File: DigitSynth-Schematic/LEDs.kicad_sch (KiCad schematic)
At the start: 0 parts

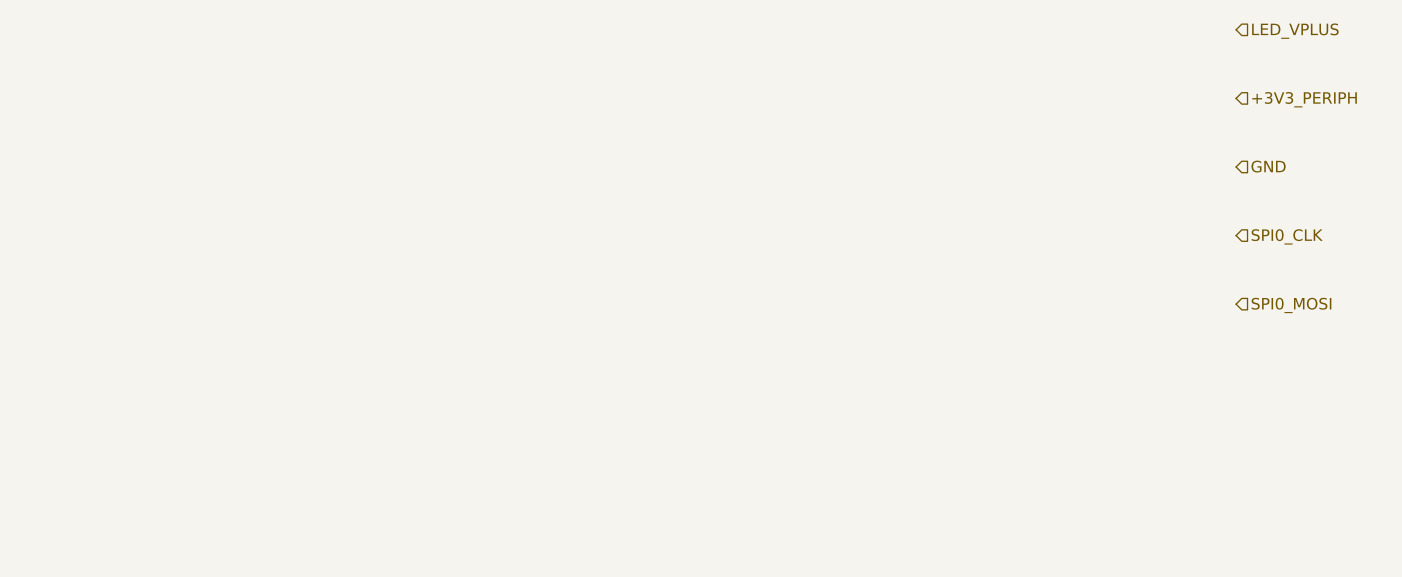
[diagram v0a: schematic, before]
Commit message: Add completed KiCad schematic hierarchy (Pi interface, ADC, LEDs, buttons, power)
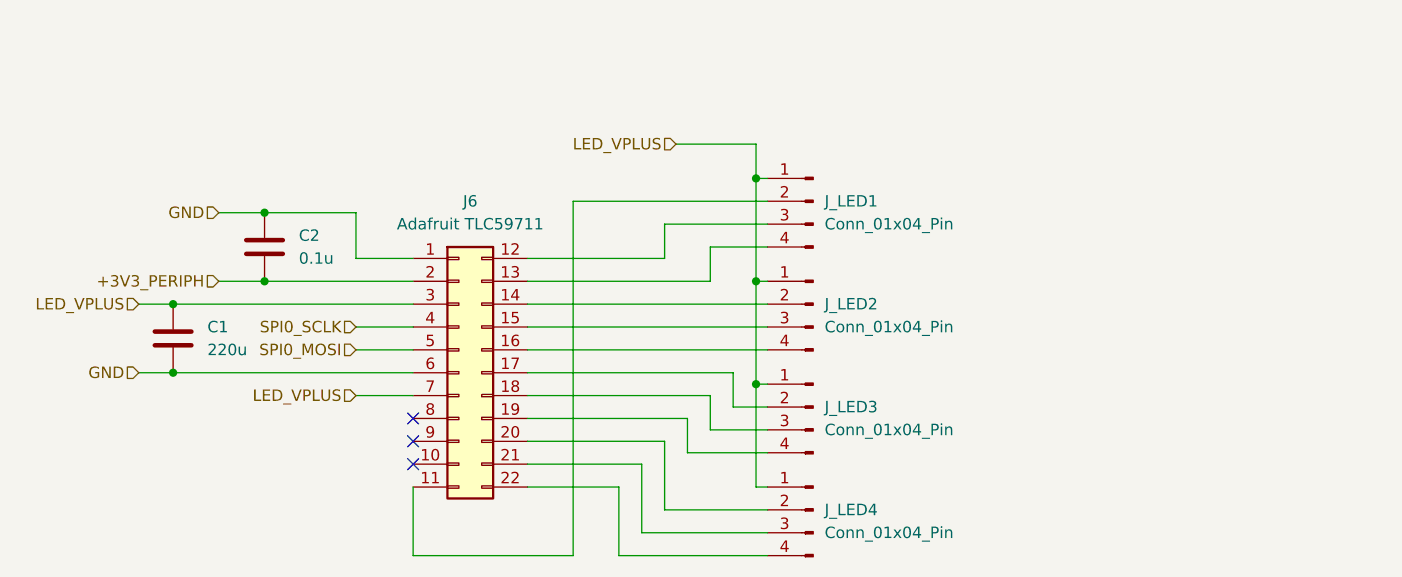
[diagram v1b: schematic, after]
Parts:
- added C1: 220u, symbol Device:C
- added C2: 0.1u, symbol Device:C
- added J6: Adafruit TLC59711, symbol Connector_Generic:Conn_02x11_Top_Bottom
- added J_LED1, J_LED2, J_LED3, J_LED4: Conn_01x04_Pin, symbol Connector:Conn_01x04_Pin
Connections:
- net +3V3_PERIPH: now also C2.2, J6.2 (+3V3_PERIPH)
- net GND: now also C1.2, C2.1, J6.1 (GND), J6.6 (GND)
- net LED_VPLUS: now also C1.1, J6.3 (LED_VPLUS), J6.7 (LED_VPLUS), J_LED1.1 (LED_VPLUS), J_LED2.1 (LED_VPLUS), J_LED3.1 (LED_VPLUS), J_LED4.1 (LED_VPLUS)
- net SPI0_MOSI: now also J6.5 (SPI0_MOSI)
- new net: J6.11 (LED1_R), J_LED1.2 (LED_R)
- new net: J6.12 (LED1_G), J_LED1.3 (LED_G)
- new net: J6.13 (LED1_B), J_LED1.4 (LED_VPLUS)
- new net: J6.20 (LED4_R), J_LED4.2 (LED_R)
- new net: J6.21 (LED4_G), J_LED4.3 (LED_G)
- new net: J6.22 (Pin_22), J_LED4.4 (LED_VPLUS)
- new net: J6.17 (LED3_R), J_LED3.2 (LED_R)
- new net: J6.18 (LED3_G), J_LED3.3 (LED_G)
- new net: J6.19 (LED3_B), J_LED3.4 (LED_VPLUS)
- new net: J6.14 (LED2_R), J_LED2.2 (LED_R)
- new net: J6.15 (LED2_G), J_LED2.3 (LED_G)
- new net: J6.16 (LED2_B), J_LED2.4 (LED_VPLUS)
- new net SPI0_SCLK: J6.4 (SPI0_SCLK)
- no-connect marks 0 -> 3
